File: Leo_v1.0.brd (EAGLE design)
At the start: 68.6 x 53.3 mm, 56 parts, among them CN1 POWER_JACK, CN2 47346-0001, CN3 DIGITAL10, CN4 DIGITAL8, CN5 ICSP, CN6 POWER8, CN7 ANALOG6, IC1 AMS1117-5.0, IC2 AMS1117-3.3, IC3 MCP6002T-I/SN, Q2 16MHz, T1 AO3401A, T2 2N7002, U1 ATMEGA32U4-MU, U2 ATMEGA32U4-AU

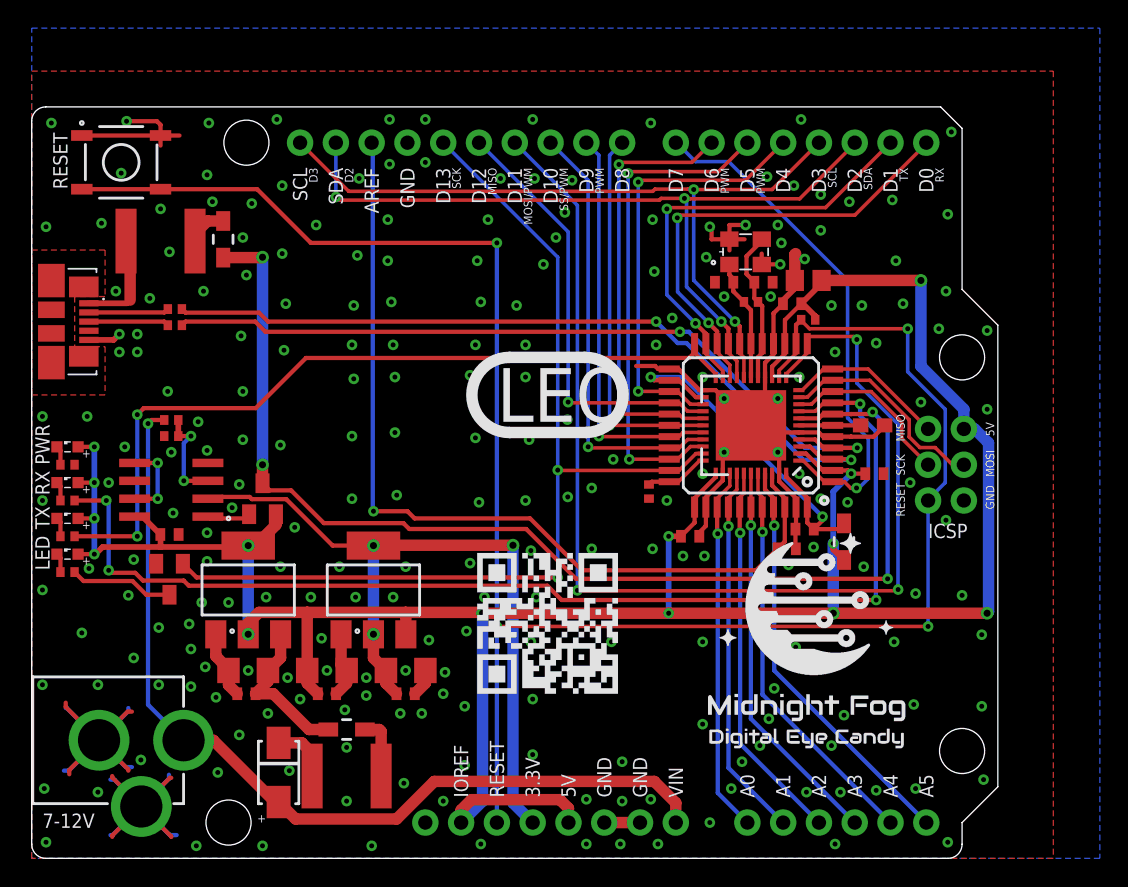
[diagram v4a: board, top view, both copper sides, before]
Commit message: Moved few traces around.
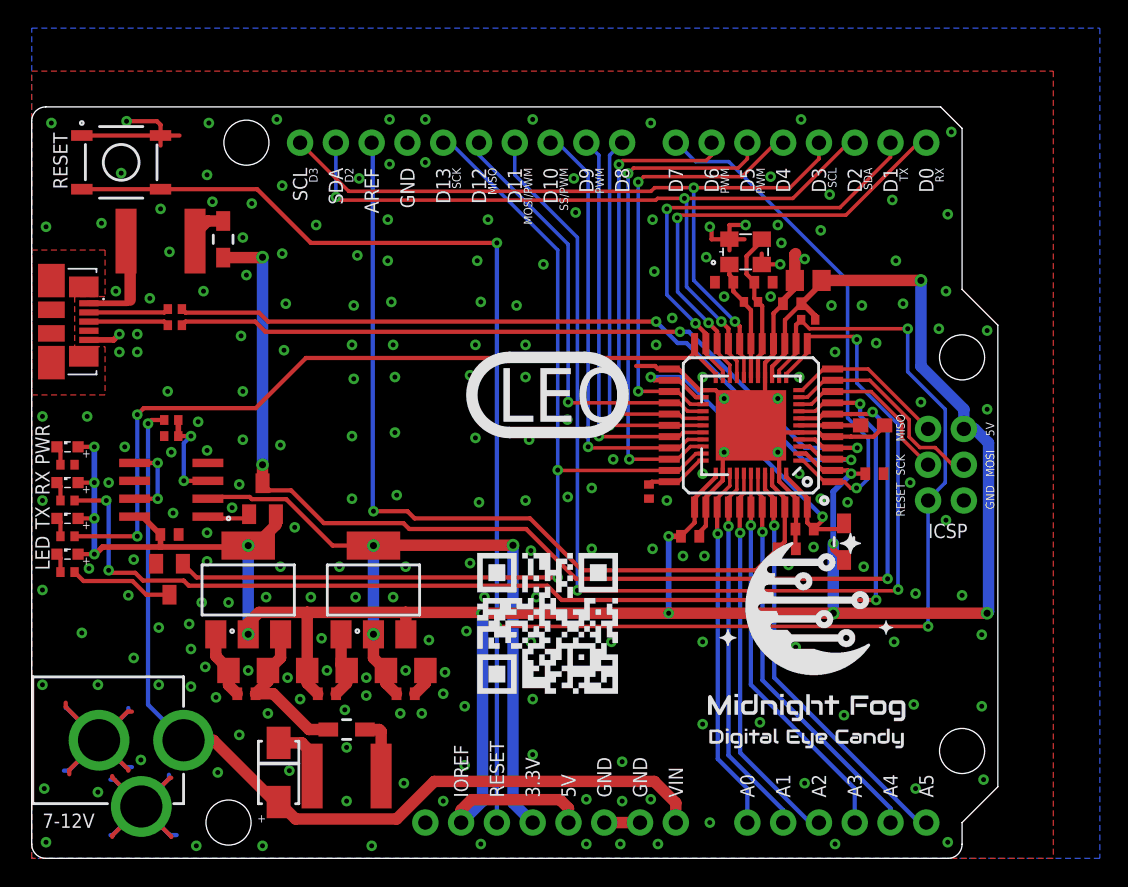
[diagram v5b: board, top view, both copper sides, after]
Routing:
- net D3_SCL: track 54.5 -> 55.3 mm
- net D5_PWM: track 35.3 -> 36.0 mm
- net D1_TX: track 31.4 -> 32.0 mm
- net D6_PWM: track 31.1 -> 31.6 mm
- net GND: vias 236 -> 224
